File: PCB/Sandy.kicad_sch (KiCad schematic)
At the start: 156 parts, among them J1 USB_C_Receptacle_USB2.0, J2 Conn_01x03, J3 Conn_01x02, J4 Conn_02x03_Odd_Even, J5 Conn_02x02_Top_Bottom, J6 Conn_02x02_Top_Bottom, J7 Conn_02x02_Top_Bottom, J8 Conn_02x02_Top_Bottom, U1 ATmega32U4-MU, U2 24LC64, Y1 16MHz

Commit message: コネクタ位置考え中
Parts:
- added J10, J15, J16, J9: Conn_01x04, Connector_PinHeader_2.54mm:PinHeader_1x04_P2.54mm_Vertical, symbol Connector_Generic:Conn_01x04
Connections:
- net MISO: now also J10.4 (Pin_4)
- net MOSI: now also J10.2 (Pin_2)
- net RE_L1_1: now also J9.2 (Pin_2)
- net RE_R1_1: now also J16.4 (Pin_4)
- net RE_R2_1: now also J15.2 (Pin_2)
- net SCK: now also J9.4 (Pin_4)
- net col5: now also J15.4 (Pin_4)
- net col6: now also J16.2 (Pin_2)
- net row0: now also J9.1 (Pin_1)
- net row1: now also J10.1 (Pin_1)
- net row2: now also J15.1 (Pin_1)
- net row3: now also J16.1 (Pin_1)
- net row5: now also J9.3 (Pin_3)
- net row6: now also J10.3 (Pin_3)
- net row7: now also J15.3 (Pin_3)
- net row8: now also J16.3 (Pin_3)
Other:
- note added: "Spare pin & Virtual Connection"
- note removed: "Virtual Connection"

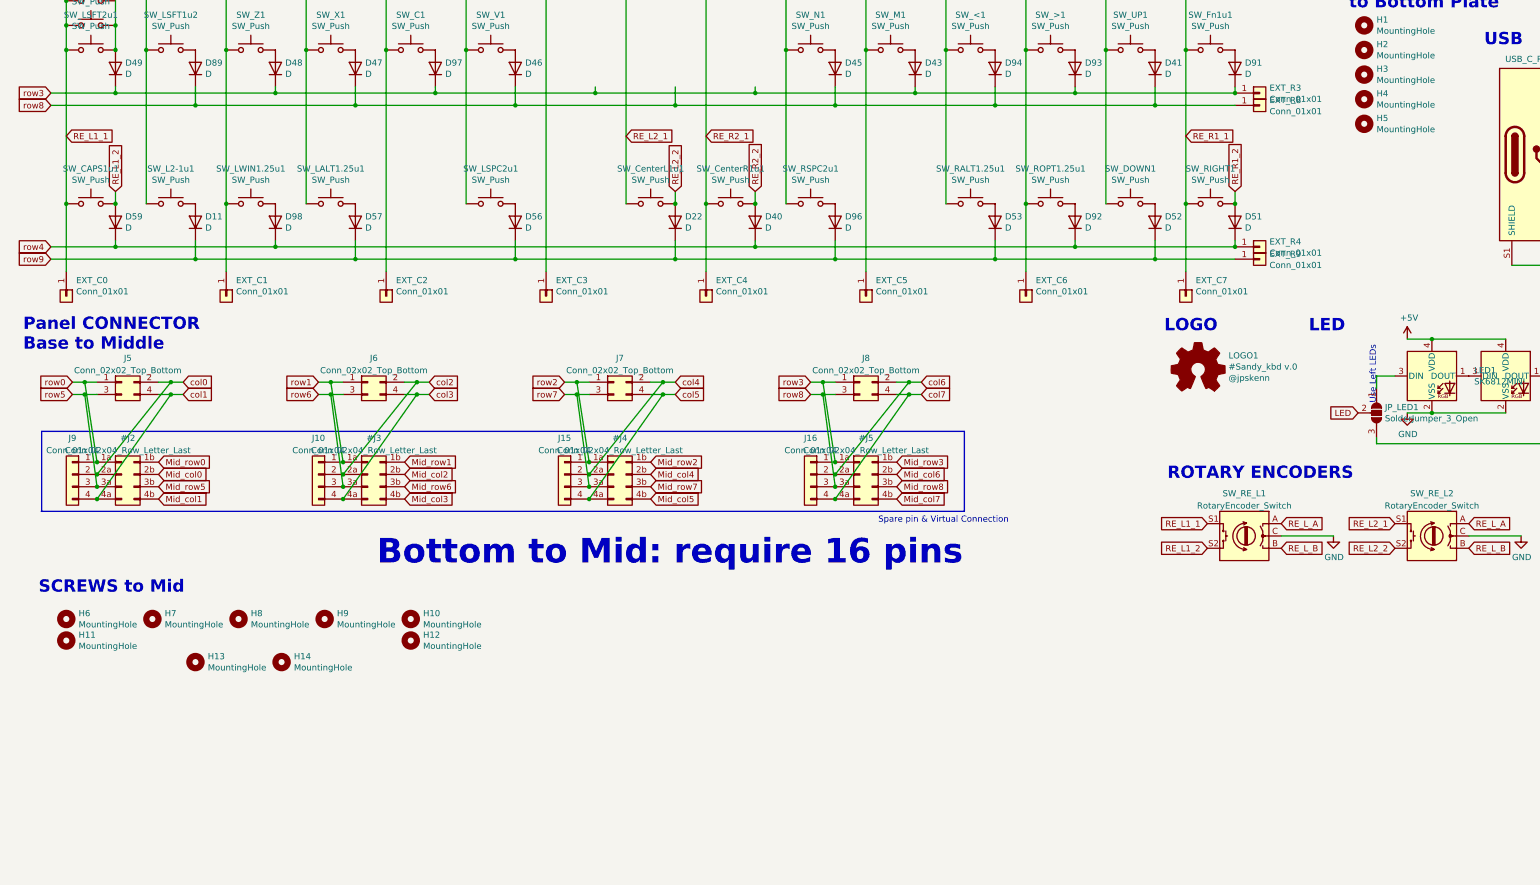
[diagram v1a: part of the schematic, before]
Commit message: 3枚の基板を1枚にまとめ中
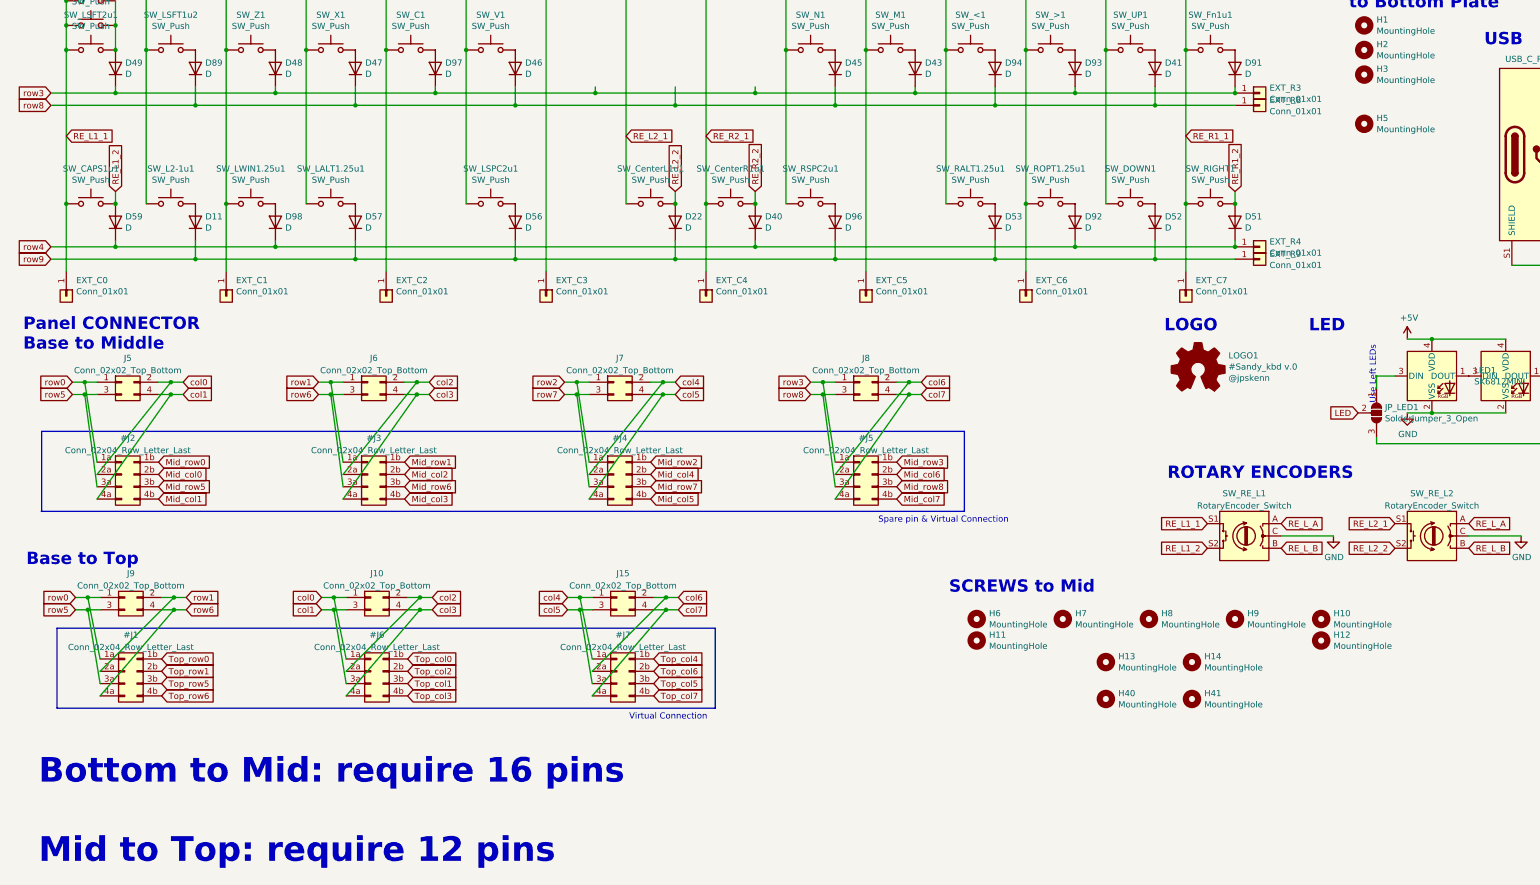
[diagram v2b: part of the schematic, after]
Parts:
- removed H4: MountingHole, MountingHole:MountingHole_2.2mm_M2_No_Cu, symbol Mechanical:MountingHole
- removed J10, J15, J16, J9: Conn_01x04, Connector_PinHeader_2.54mm:PinHeader_1x04_P2.54mm_Vertical, symbol Connector_Generic:Conn_01x04
- added #J1, #J6, #J7: Conn_02x04_Row_Letter_Last, symbol Connector_Generic:Conn_02x04_Row_Letter_Last
- added H40, H41: MountingHole, MountingHole:MountingHole_2.2mm_M2_No_Cu, symbol Mechanical:MountingHole
- added J10, J15, J9: Conn_02x02_Top_Bottom, locallib:JST_SH_SM04B-SRSS-TB_1x04-1MP_P1.00mm_Horizontal_wCable_housing_spare_pin, symbol Connector_Generic:Conn_02x02_Odd_Even
- J5, J6, J7, J8: footprint Connector_JST:JST_SH_SM04B-SRSS-TB_1x04-1MP_P1.00mm_Horizontal -> locallib:JST_SH_SM04B-SRSS-TB_1x04-1MP_P1.00mm_Horizontal_wCable_housing_spare_pin
- SW_LSFT2u1: footprint MX_Alps_Hybrid:MXOnly-2U-Hotswap-guide -> MX_Alps_Hybrid:MXOnly-2U-Hotswap-guide2
- SW_LSPC2u1, SW_RSPC2u1: footprint MX_Alps_Hybrid:MXOnly-2U-Hotswap-ReversedStabilizers-guide -> MX_Alps_Hybrid:MXOnly-2U-Hotswap-ReversedStabilizers-guide2
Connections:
- net MISO: now also #J6.4a (Pin_4a), J10.4 (Pin_4)
- net MOSI: now also #J6.2a (Pin_2a), J10.2 (Pin_2)
- net RE_L1_1: now also #J6.1a (Pin_1a), J10.1 (Pin_1)
- net RE_R1_1: now also #J7.4a (Pin_4a), J15.4 (Pin_4)
- net RE_R2_1: now also #J7.1a (Pin_1a), J15.1 (Pin_1)
- net SCK: now also #J6.3a (Pin_3a), J10.3 (Pin_3)
- net col5: now also #J7.3a (Pin_3a), J15.3 (Pin_3)
- net col6: now also #J7.2a (Pin_2a), J15.2 (Pin_2)
- net row0: now also #J1.1a (Pin_1a), J9.1 (Pin_1)
- net row1: now also #J1.2a (Pin_2a), J9.2 (Pin_2)
- net row5: now also #J1.3a (Pin_3a), J9.3 (Pin_3)
- net row6: now also #J1.4a (Pin_4a), J9.4 (Pin_4)
- new net Top_col0: #J6.1b (Pin_1b)
- new net Top_col1: #J6.3b (Pin_3b)
- new net Top_col2: #J6.2b (Pin_2b)
- new net Top_col3: #J6.4b (Pin_4b)
- new net Top_col4: #J7.1b (Pin_1b)
- new net Top_col5: #J7.3b (Pin_3b)
- new net Top_col6: #J7.2b (Pin_2b)
- new net Top_col7: #J7.4b (Pin_4b)
- new net Top_row0: #J1.1b (Pin_1b)
- new net Top_row1: #J1.2b (Pin_2b)
- new net Top_row5: #J1.3b (Pin_3b)
- new net Top_row6: #J1.4b (Pin_4b)
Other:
- note added: "Base to Top"
- note added: "Bottom to Mid: require 16 pins Mid to Top: require 12 pins"
- note added: "Virtual Connection"
- note removed: "Bottom to Mid: require 16 pins"
- moved on the sheet: H10, H11, H12, H13, H14, H6, H7, H8, H9

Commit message: 基板外形置き換え
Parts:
- added #J8: Conn_02x02_Row_Letter_Last, symbol Connector_Generic:Conn_02x02_Row_Letter_Last
- H10, H11, H12, H13, H14, H40, H41, H6, H7, H8, H9: footprint MountingHole:MountingHole_2.2mm_M2_No_Cu -> MountingHole:MountingHole_2.2mm_M2_Pad; symbol Mechanical:MountingHole -> Mechanical:MountingHole_Pad
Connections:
- net GND: now also H10.1, H11.1, H12.1, H13.1, H14.1, H40.1, H41.1, H6.1, H7.1, H8.1, H9.1, #J8.1a (Pin_1a), #J8.2a (Pin_2a)
- new net Mid_GND: #J8.1b (Pin_1b)
- new net Top_GND: #J8.2b (Pin_2b)

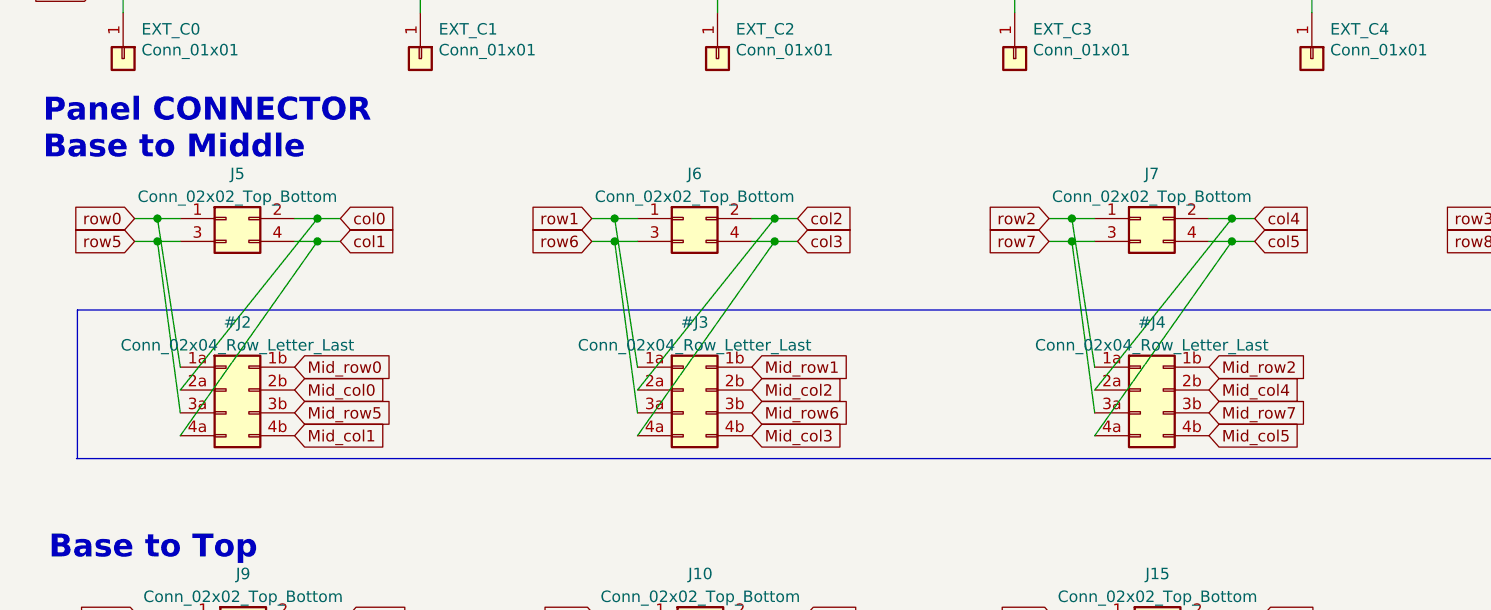
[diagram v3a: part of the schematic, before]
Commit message: BaseからMidへのピン数減少のため、コネクタ1個減らす
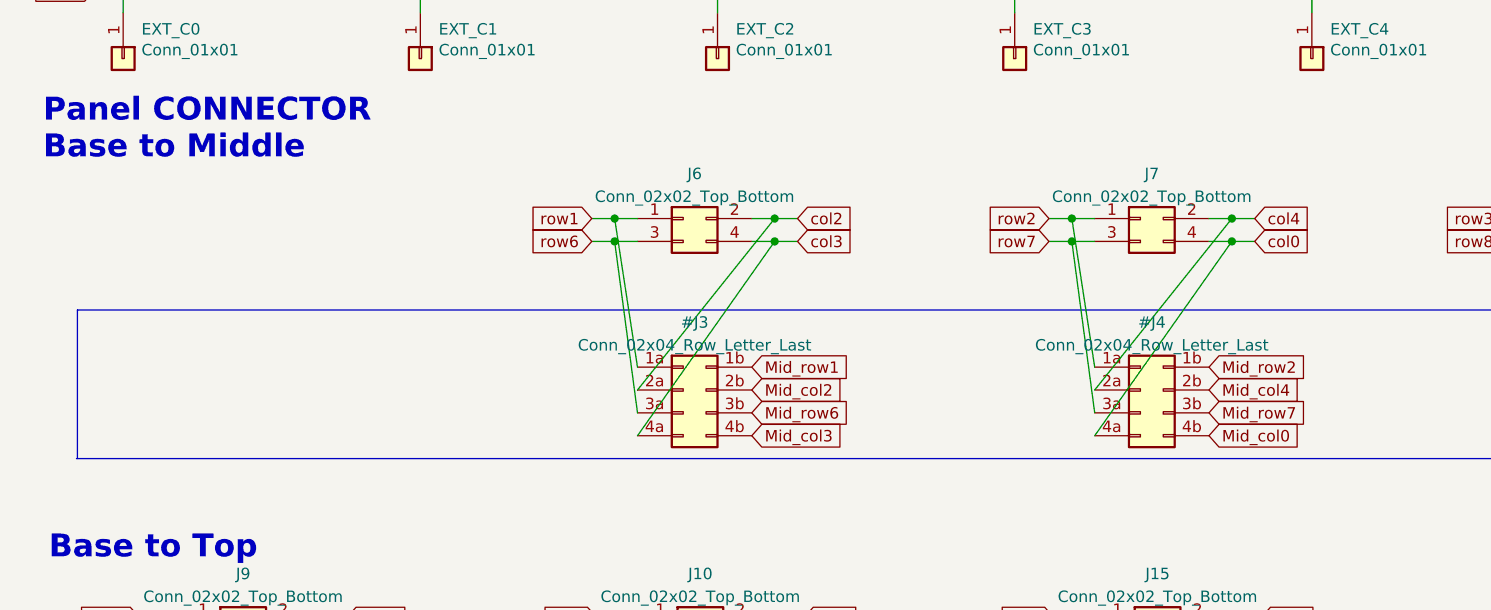
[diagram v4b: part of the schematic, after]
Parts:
- removed #J2: Conn_02x04_Row_Letter_Last, symbol Connector_Generic:Conn_02x04_Row_Letter_Last
- removed J5: Conn_02x02_Top_Bottom, locallib:JST_SH_SM04B-SRSS-TB_1x04-1MP_P1.00mm_Horizontal_wCable_housing_spare_pin, symbol Connector_Generic:Conn_02x02_Odd_Even
- H10, H11, H12, H13, H14, H40, H41, H6, H7, H8, H9: footprint MountingHole:MountingHole_2.2mm_M2_Pad -> MountingHole:MountingHole_2.2mm_M2_Pad_minimal
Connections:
- net Mid_col5 is gone; now on net Mid_col0: #J4.4b (Pin_4b)
- net RE_L1_1: now also #J4.4a (Pin_4a), J7.4 (Pin_4)
- net col5: no longer #J4.4a (Pin_4a), J7.4 (Pin_4)

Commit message: スイッチのソケットを廃止
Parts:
- SW_;1, SW_<1, SW_>1, SW_A1, SW_C1, SW_D1, SW_DOWN1, SW_E1, SW_F1, SW_Fn1u1, SW_I1, SW_J1, SW_K1, SW_L1, SW_L2-1u1, SW_LSFT1u1, SW_LSFT1u2, SW_M1, SW_N1, SW_O1, SW_S1, SW_UP1, SW_V1, SW_W1, SW_X1, SW_Z1: footprint MX_Alps_Hybrid:MXOnly-1U-Hotswap-guide -> MX_Alps_Hybrid:MXOnly-1U-NoLED
- SW_CAPS1u1, SW_CenterL1u1, SW_CenterR1u1, SW_RIGHT1: footprint MX_Alps_Hybrid:MXOnly-1U-Hotswap-on-RE-guide -> MX_Alps_Hybrid:MXOnly-1U-NoLED
- SW_CTL1.25u1, SW_ENT1.25u1, SW_LALT1.25u1, SW_LWIN1.25u1, SW_RALT1.25u1, SW_ROPT1.25u1: footprint MX_Alps_Hybrid:MXOnly-1.25U-Hotswap-guide -> MX_Alps_Hybrid:MXOnly-1.25U-NoLED
- SW_CTL1.5u1, SW_ENT1.5u1: footprint MX_Alps_Hybrid:MXOnly-1.5U-Hotswap-guide -> MX_Alps_Hybrid:MXOnly-1.5U-NoLED
- SW_LSFT2u1: footprint MX_Alps_Hybrid:MXOnly-2U-Hotswap-guide2 -> MX_Alps_Hybrid:MXOnly-2U-NoLED
- SW_LSPC2u1, SW_RSPC2u1: footprint MX_Alps_Hybrid:MXOnly-2U-Hotswap-ReversedStabilizers-guide2 -> MX_Alps_Hybrid:MXOnly-2U-ReversedStabilizers-NoLED
